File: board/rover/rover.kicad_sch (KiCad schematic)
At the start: 1 part, among them IC1 DRV5053RAQLPG

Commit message: Finished PCB
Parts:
- removed IC1: DRV5053RAQLPG, LP0003A, symbol DRV5053RAQLPG:DRV5053RAQLPG
- added C1, C5, Cbp1, Cbp2, Cbp3, Cbp4, Chpf1, Cth1: 100n, Capacitor_THT:C_Disc_D5.0mm_W2.5mm_P2.50mm, symbol Device:C
- added C2, C3, Cin1, Clpf1: 10n, Capacitor_THT:C_Disc_D5.0mm_W2.5mm_P2.50mm, symbol Device:C
- added C6: 10u, Capacitor_THT:CP_Radial_D5.0mm_P2.50mm, symbol Device:C
- added COIL_IN1, IR_IN1, US_IN1: Conn_01x02, TerminalBlock:TerminalBlock_MaiXu_MX126-5.0-02P_1x02_P5.00mm, symbol Connector_Generic:Conn_01x02
- added Cf1: 100p, Capacitor_THT:C_Disc_D5.0mm_W2.5mm_P2.50mm, symbol Device:C
- added D4, D5: 1N914, Diode_THT:D_DO-35_SOD27_P7.62mm_Horizontal, symbol Diode:1N914
- added MAG_IN1, METRO_OUT1, PWR_IN1: 2212S-04SG-85, header1x4:2212S04SG85, symbol 2212S-04SG-85:2212S-04SG-85
- added R1, R3: 19k, Resistor_THT:R_Axial_DIN0207_L6.3mm_D2.5mm_P10.16mm_Horizontal, symbol Device:R
- added R2, R4, Rf12, Rf22, Rf23: 1k, Resistor_THT:R_Axial_DIN0207_L6.3mm_D2.5mm_P10.16mm_Horizontal, symbol Device:R
- added R7, Rb11, Rg1, Rhpf1, Rpullup1, Rth1, Rth2: 10k, Resistor_THT:R_Axial_DIN0207_L6.3mm_D2.5mm_P10.16mm_Horizontal, symbol Device:R
- added RL1: 20k, Resistor_THT:R_Axial_DIN0207_L6.3mm_D2.5mm_P10.16mm_Horizontal, symbol Device:R
- added Rb12: 1.5k, Resistor_THT:R_Axial_DIN0207_L6.3mm_D2.5mm_P10.16mm_Horizontal, symbol Device:R
- added Rf1: 91k, Resistor_THT:R_Axial_DIN0207_L6.3mm_D2.5mm_P10.16mm_Horizontal, symbol Device:R
- added Rf11, Rf21: 9k, Resistor_THT:R_Axial_DIN0207_L6.3mm_D2.5mm_P10.16mm_Horizontal, symbol Device:R
- added Rhyst1: 1Meg, Resistor_THT:R_Axial_DIN0207_L6.3mm_D2.5mm_P10.16mm_Horizontal, symbol Device:R
- added U1, U3: MCP6022, MCP6022:PDIP8_300MC_MCH, symbol Amplifier_Operational:MCP6022
- added U2: LM393, LM393P:P8, symbol Comparator:LM393
- added U4: TLE2072CP, TLE2072CP:P8, symbol 2026-06-04_15-17-56:TLE2072CP
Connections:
- net +3.3V: now also C5.1, C6.1, Cbp4.2, IR_IN1.1 (Pin_1), MAG_IN1.1, PWR_IN1.3, Rb11.1, Rpullup1.2, Rth1.1, U1.8 (V+), U2.8 (V+), U3.8 (V+)
- net GND: now also C2.2, C3.2, C5.2, C6.2, COIL_IN1.2 (Pin_2), Cbp1.2, Cbp2.2, Cbp3.2, Cbp4.1, Clpf1.2, Cth1.2, MAG_IN1.2, PWR_IN1.4, R2.1, R4.2, R7.2, RL1.2, Rb12.2, Rf23.1, Rg1.2, Rth2.2, U1.4 (V-), U2.4 (V-), U3.4 (V-), US_IN1.1 (Pin_1)
- new net: C1.1, Clpf1.1, IR_IN1.2 (Pin_2), RL1.1
- new net: R1.2, U4.1 (1OUT), U4.5 (2IN+)
- new net: R1.1, R2.2, U4.2 (1IN-)
- new net: C2.1, COIL_IN1.1 (Pin_1), U4.3 (1IN+)
- new net: R3.2, R4.1, U4.6 (2IN-)
- new net: D4.2 (A), R3.1, U4.7 (2OUT)
- new net: Cf1.1, Rf1.1, Rg1.1, U1.2 (-)
- new net: Cf1.2, Chpf1.1, Rf1.2, U1.1
- new net: Rf11.1, U3.1, U3.5 (+)
- new net: Rf11.2, Rf12.2, U3.2 (-)
- new net: Cin1.1, Rb11.2, Rb12.1, U3.3 (+)
- new net: Cbp1.1, Rf12.1
- new net: Cth1.1, Rhpf1.2, Rth1.2, Rth2.1, U2.2 (-)
- new net: Chpf1.2, Rhpf1.1, Rhyst1.1, U2.3 (+)
- new net: C1.2, U1.3 (+)
- new net: Cbp2.1, Rf22.1
- new net: Rf21.2, Rf22.2, U3.6 (-)
- new net: D5.2 (A), Rf21.1, U3.7
- new net: Cin1.2, US_IN1.2 (Pin_2)
- new net +5V: PWR_IN1.1, U4.8 (VCC+)
- new net -5V: PWR_IN1.2, U4.4 (VCC-)
- new net AGE_OUT: C3.1, D4.1 (K), METRO_OUT1.1, R7.1
- new net IR_OUT: METRO_OUT1.2, Rhyst1.2, Rpullup1.1, U2.1
- new net MAG_OUT: MAG_IN1.3, METRO_OUT1.4
- new net US_OUT: Cbp3.1, D5.1 (K), METRO_OUT1.3, Rf23.2
- no-connect marks 0 -> 7
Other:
- note added: "AGE"
- note added: "IR"
- note added: "MAG"
- note added: "OUTPUT"
- note added: "PWR"
- note added: "US"

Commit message: Added -5V generation to PCB
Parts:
- added C7, C8: 10u, Capacitor_THT:CP_Radial_D5.0mm_P2.50mm, symbol Device:C
- added U5: icl7660cpa, ICL7660CPA:21-0043D_8_MXM, symbol 2026-06-05_10-32-33:icl7660cpa
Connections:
- net +5V: now also U5.8 (V+)
- net -5V: now also C8.1, U5.5 (VOUT)
- net GND: now also C8.2, U5.3 (GND)
- new net: C7.1, U5.2 (CAP+)
- new net: C7.2, U5.4 (CAP-)
- no-connect marks 7 -> 9
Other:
- moved on the sheet: Cbp4, MAG_IN1, METRO_OUT1, PWR_IN1

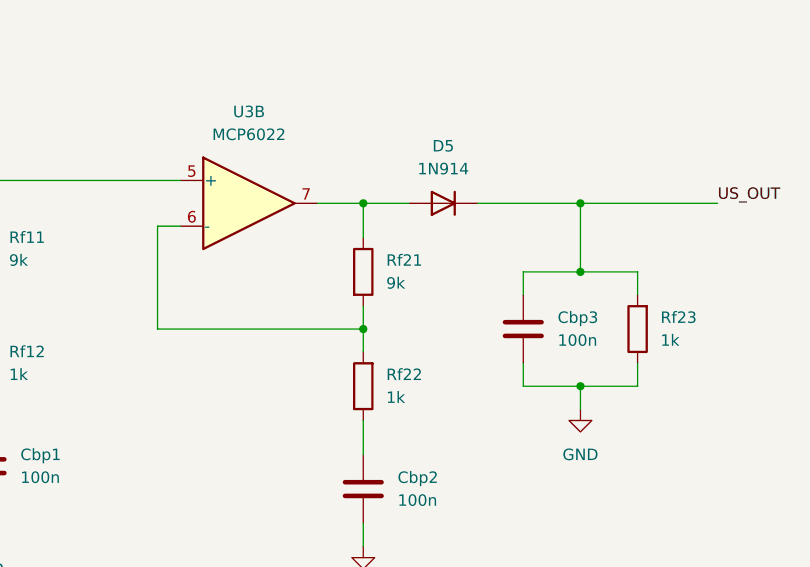
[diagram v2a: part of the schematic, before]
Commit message: Changed thresholds and added rock type panel in app
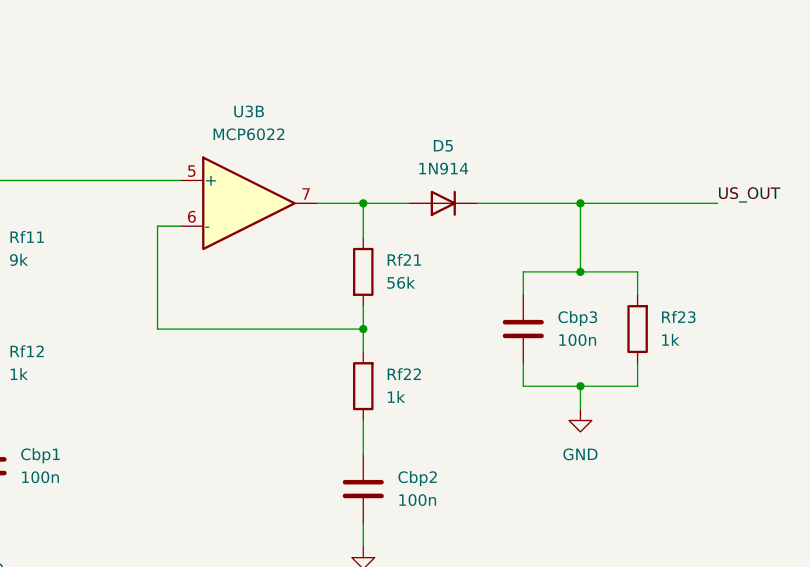
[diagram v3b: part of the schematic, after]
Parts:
- Rf21: value 9k -> 56k
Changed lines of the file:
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@@
 			)
 		)
-		(property "Value" "9k"
+		(property "Value" "56k"
 			(at 152.4 229.8699 0)
 			(show_name no)
